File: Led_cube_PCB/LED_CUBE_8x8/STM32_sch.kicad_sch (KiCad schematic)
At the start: 21 parts, among them IC29 STM32C071C8T6, IC30 TPS562202DRLR, J2 20021121-00014T4LF, Y1 ABM11-48.000MHz-D7X-T

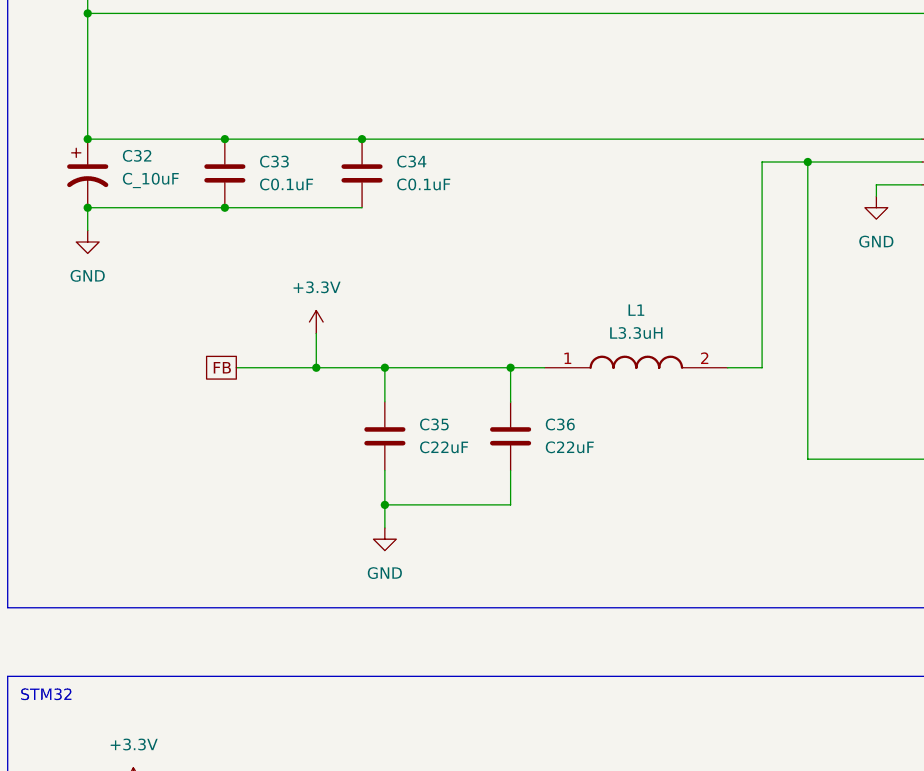
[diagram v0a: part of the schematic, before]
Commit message: Added test points and solder jumpers
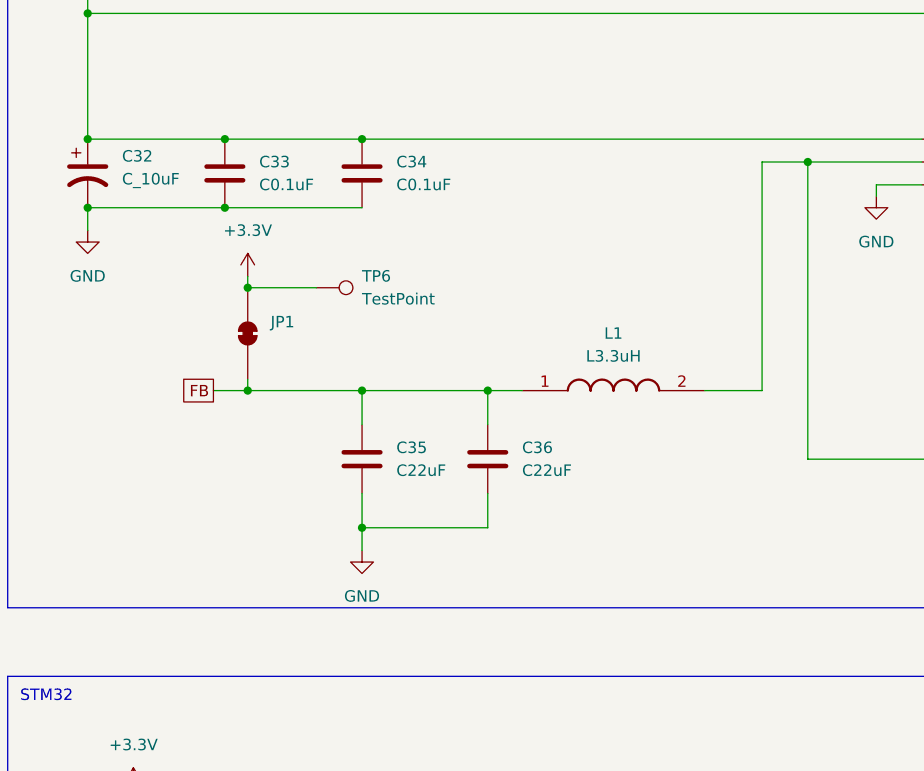
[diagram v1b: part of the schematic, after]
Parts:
- added JP1: SolderJumper_2_Bridged, Jumper:SolderJumper-2_P1.3mm_Open_RoundedPad1.0x1.5mm, symbol Jumper:SolderJumper_2_Bridged
- added TP6: TestPoint, TestPoint:TestPoint_Pad_D2.0mm, symbol Connector:TestPoint
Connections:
- net +3.3V: now also JP1.2 (B), TP6.1; no longer C35.1, C36.1, C38.1, L1.1, R57.2
- new net FB: C35.1, C36.1, C38.1, JP1.1 (A), L1.1, R57.2
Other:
- moved on the sheet: C35, C36, L1
